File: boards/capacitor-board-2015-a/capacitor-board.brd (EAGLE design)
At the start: 21.8 x 63.5 mm, 14 parts, among them Q1 FDV303N, Q2 FQT1N80

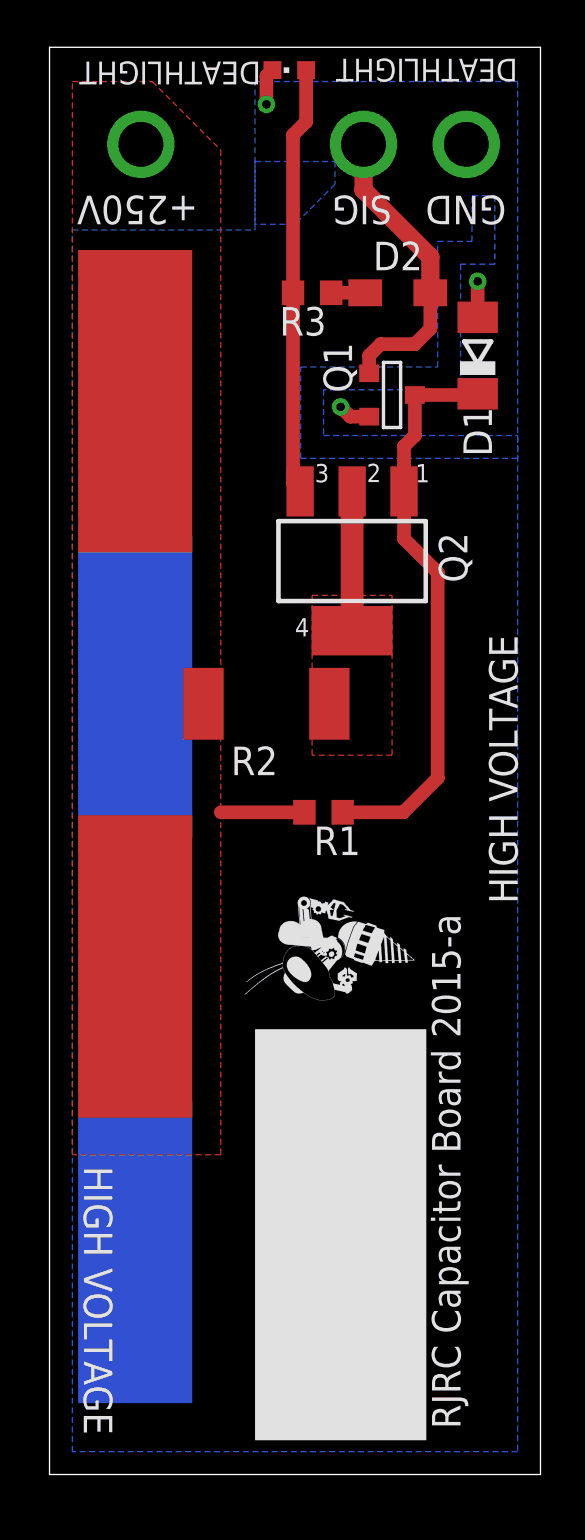
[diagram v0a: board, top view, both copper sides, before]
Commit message: capacitor-board-2015-b to capacitor-board-2015-a
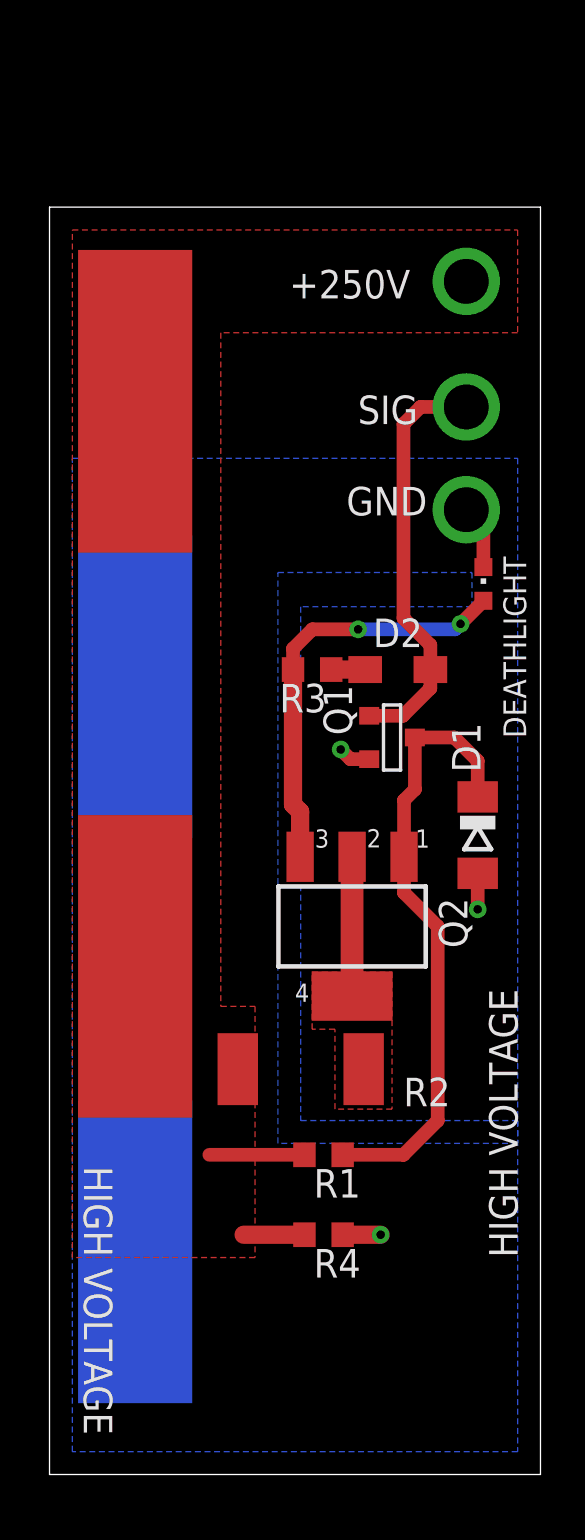
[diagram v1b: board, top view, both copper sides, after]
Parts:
- added R4: 1M, rcl:R0603
- moved DEATHLIGHT 24.4 mm to (19.3, 39.6), turned to 0 degrees
- moved D1 21.3 mm to (19.1, 28.4), turned to 270 degrees
- moved U$4 17.0 mm to (19.3, 6.10), flipped to the bottom, turned to 270 degrees
- moved D2 16.8 mm to (15.5, 35.8)
- moved R3 16.8 mm to (11.7, 35.8)
- moved R2 16.3 mm to (11.2, 18.0)
- moved Q2 16.3 mm to (13.5, 24.4)
- moved U$3 16.3 mm to (18.5, 42.9)
- moved U$1 15.7 mm to (18.5, 53.1)
- moved Q1 15.2 mm to (15.2, 32.8)
- moved R1 15.2 mm to (12.2, 14.2)
- moved U$2 12.5 mm to (18.5, 47.5)
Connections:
- net GND: now also R4.1
- net HV: now also R4.2
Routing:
- net CHARGE: track 13.4 -> 18.6 mm
- net HV: track 3.72 -> 6.94 mm
- net GND: track 4.69 -> 7.61 mm
- net N$1: track 25.5 -> 27.6 mm
- net N$3: track 19.1 -> 18.8 mm, vias 0 -> 2
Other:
- board size 21.8 x 63.5 mm -> 21.8 x 56.4 mm
- board text added: "RJRC Capacitor Board 2015-b"
- board text removed: "RJRC Capacitor Board 2015-a"
